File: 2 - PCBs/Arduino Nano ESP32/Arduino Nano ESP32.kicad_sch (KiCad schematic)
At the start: 27 parts, among them J1 USB4056-03-A, U2 MP9943GQ-Z, U3 GD25B128EWIGR

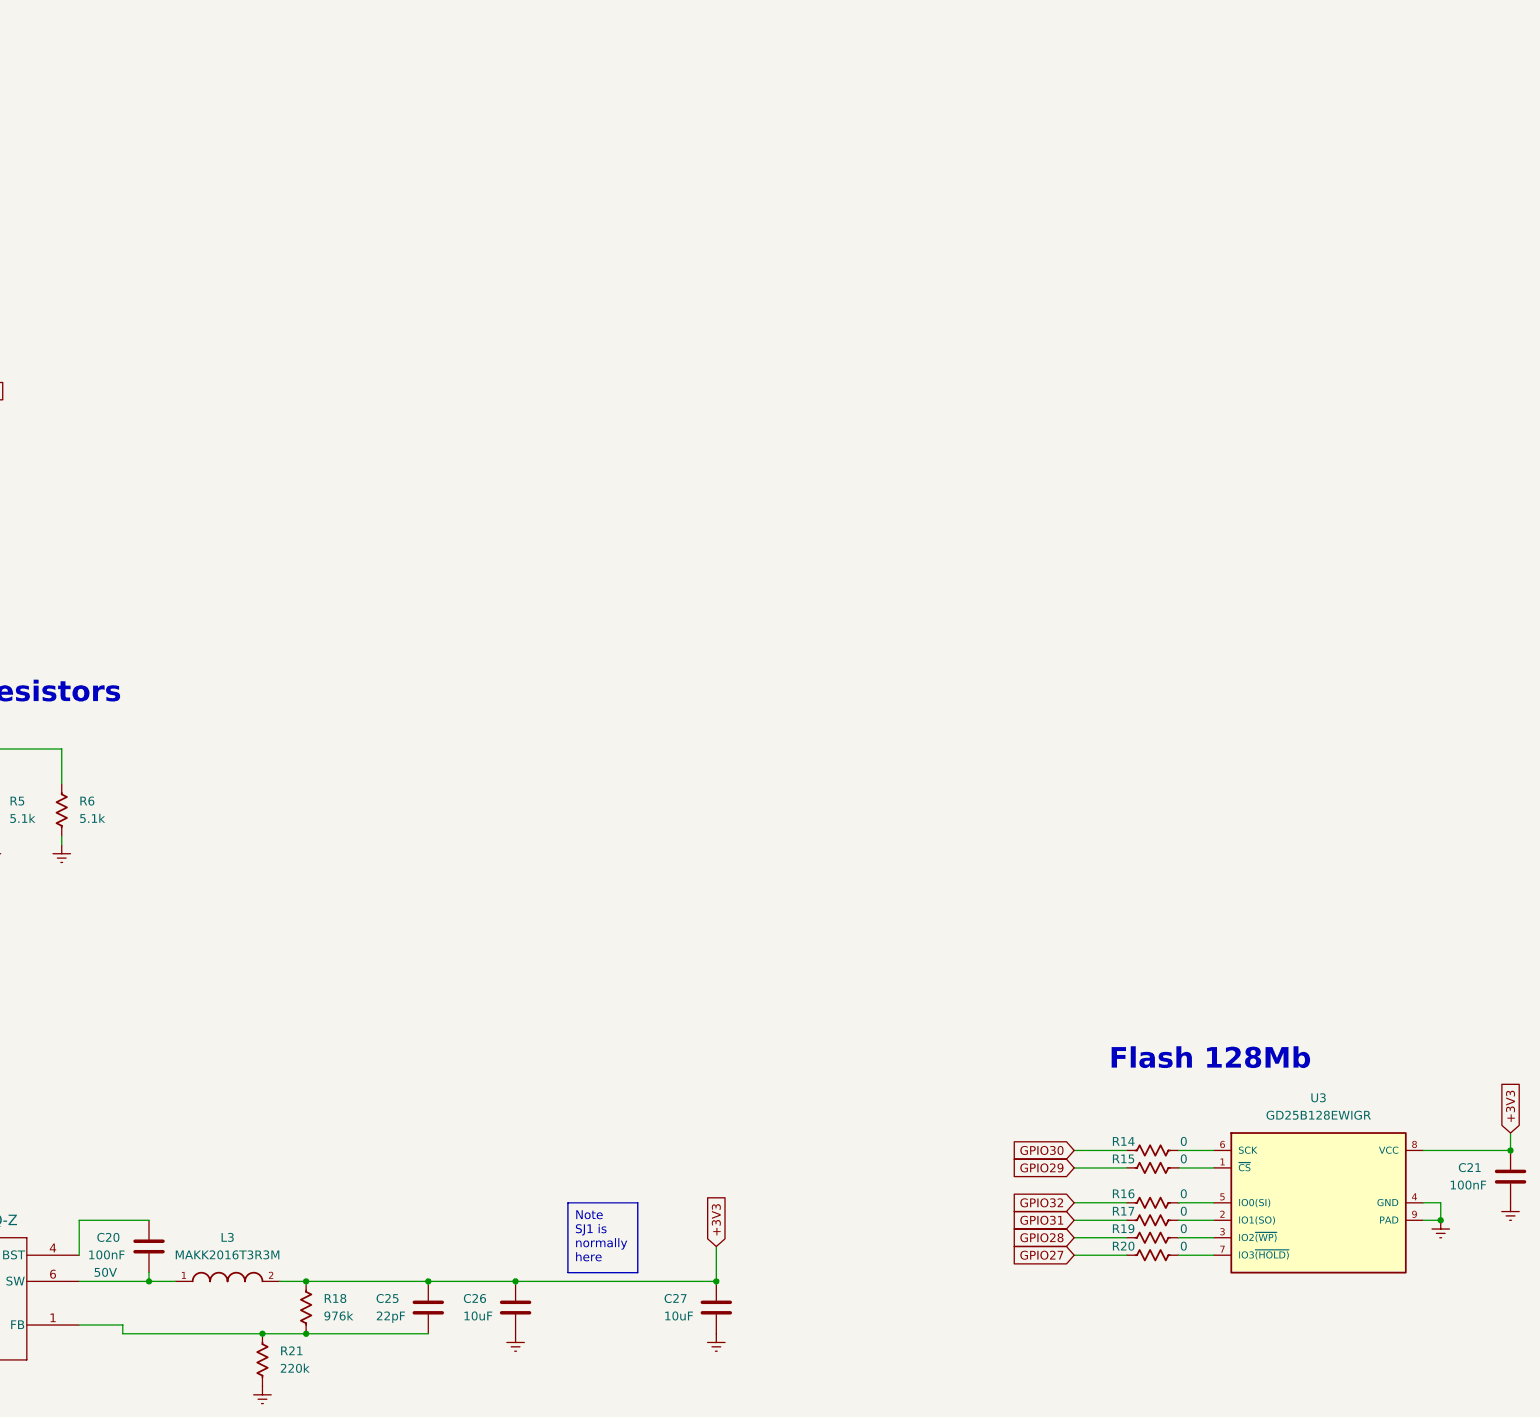
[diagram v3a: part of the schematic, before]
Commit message: Finished left side of SOC
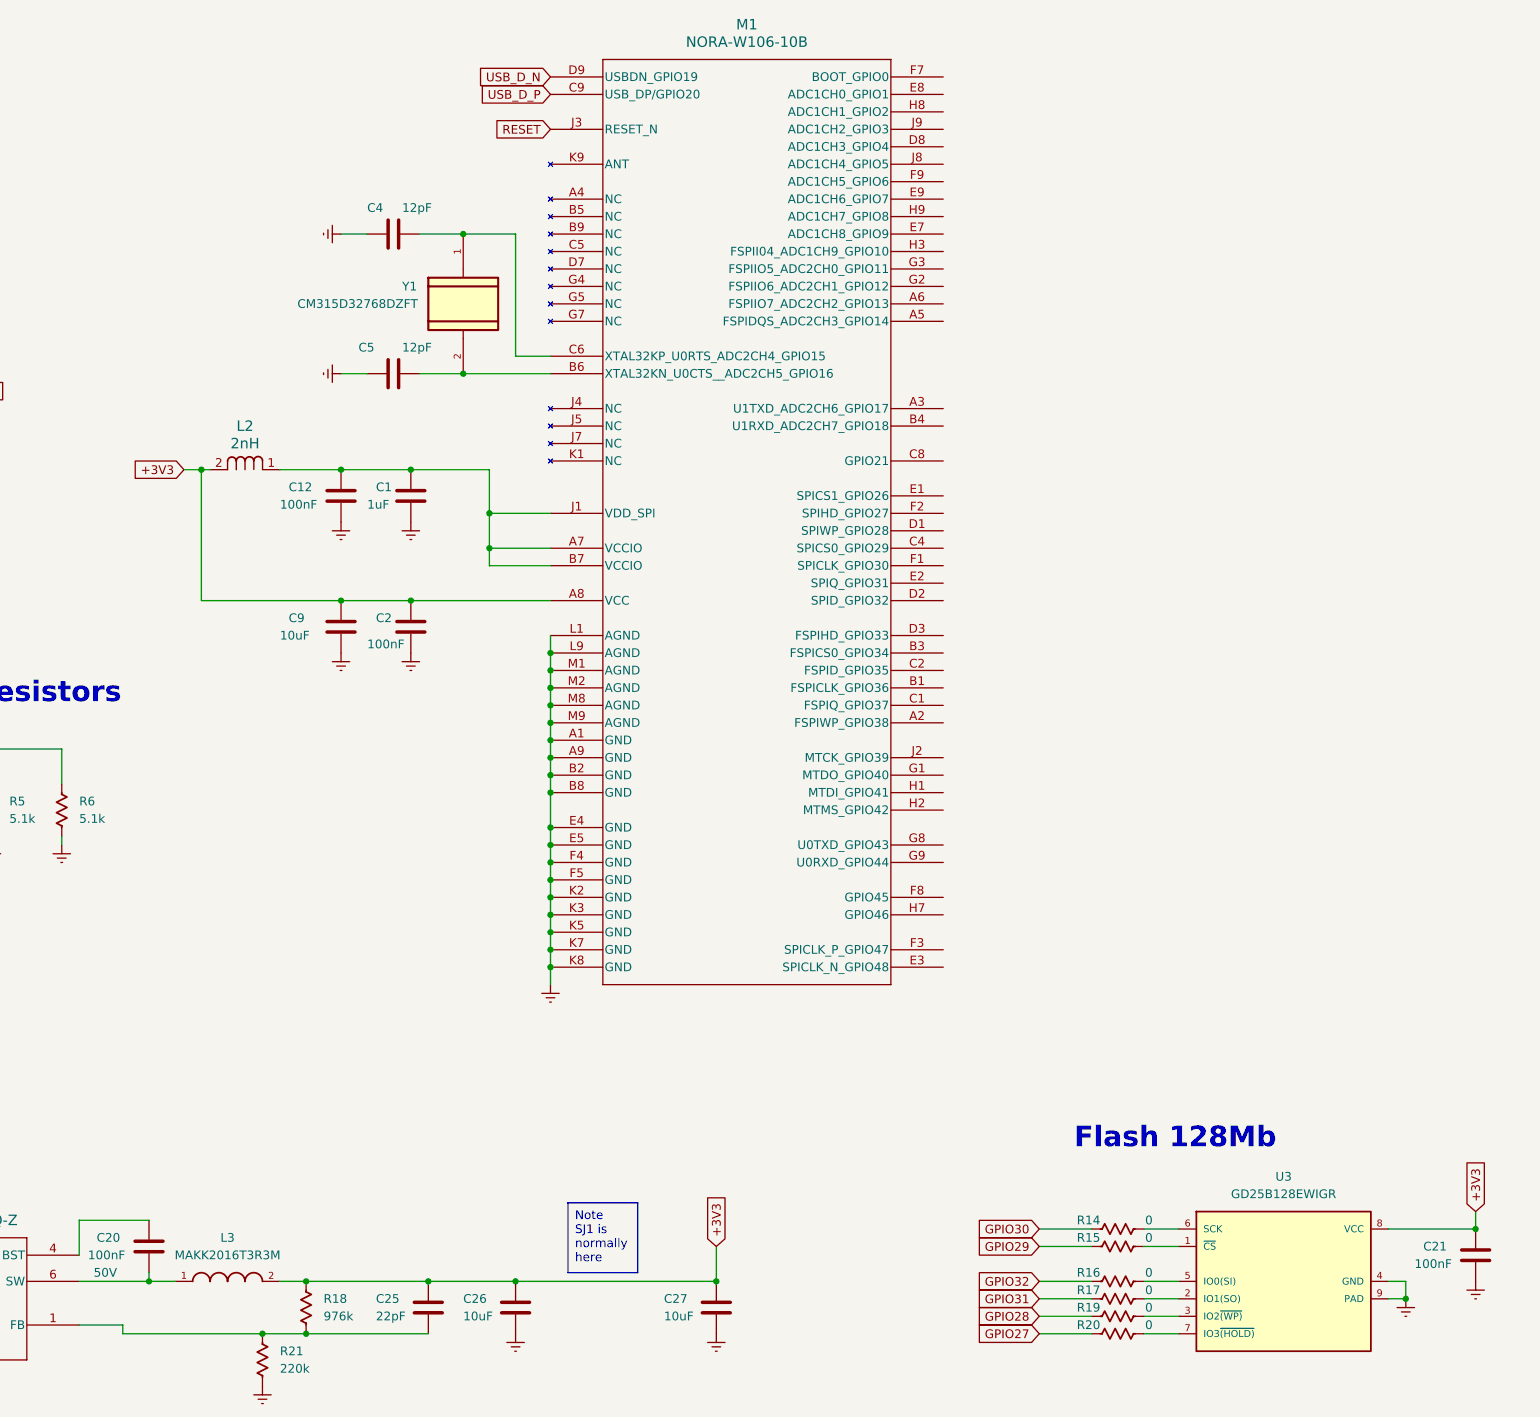
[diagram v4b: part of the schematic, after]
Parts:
- added C1: 1uF, Capacitor_SMD_AKL:C_0603_1608Metric, symbol Capacitor_US_AKL:C_0603
- added C12, C2: 100nF, Capacitor_SMD_AKL:C_0603_1608Metric, symbol Capacitor_US_AKL:C_0603
- added C4, C5: 12pF, Capacitor_SMD_AKL:C_0603_1608Metric, symbol Capacitor_US_AKL:C_0603
- added C9: 10uF, Capacitor_SMD_AKL:C_0603_1608Metric, symbol Capacitor_US_AKL:C_0603
- added L2: 2nH, 0603_inductor:0603_inductor, symbol 0603_inductor:0603_inductor
- added M1: NORA-W106-10B, NORA-W106-00B:NORA-W106-00B, symbol NORA_W106_00B:NORA-W106-00B
- added Y1: CM315D32768DZFT, CM315D32768DZFT:CM315D32768DZFT, symbol CM315D32768DZFT:CM315D32768DZFT
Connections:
- net +3V3: now also C2.1, C9.1, L2.2, M1.A8 (VCC)
- net Earth: now also C1.2, C12.2, C2.2, C4.2, C5.2, C9.2, M1.A1 (GND), M1.A9 (GND), M1.B2 (GND), M1.B8 (GND), M1.E4 (GND), M1.E5 (GND), M1.F4 (GND), M1.F5 (GND), M1.K2 (GND), M1.K3 (GND), M1.K5 (GND), M1.K7 (GND), M1.K8 (GND), M1.L1 (AGND), M1.L9 (AGND), M1.M1 (AGND), M1.M2 (AGND), M1.M8 (AGND), M1.M9 (AGND)
- net USB_D_N: now also M1.D9 (USBDN_GPIO19)
- net USB_D_P: now also M1.C9 (USB_DP/GPIO20)
- new net: C4.1, M1.C6 (XTAL32KP_U0RTS_ADC2CH4_GPIO15), Y1.1
- new net: C5.1, M1.B6 (XTAL32KN_U0CTS__ADC2CH5_GPIO16), Y1.2
- new net: C1.1, C12.1, L2.1, M1.A7 (VCCIO), M1.B7 (VCCIO), M1.J1 (VDD_SPI)
- new net RESET: M1.J3 (RESET_N)
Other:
- moved on the sheet: C21, R14, R15, R16, R17, R19, R20, U3

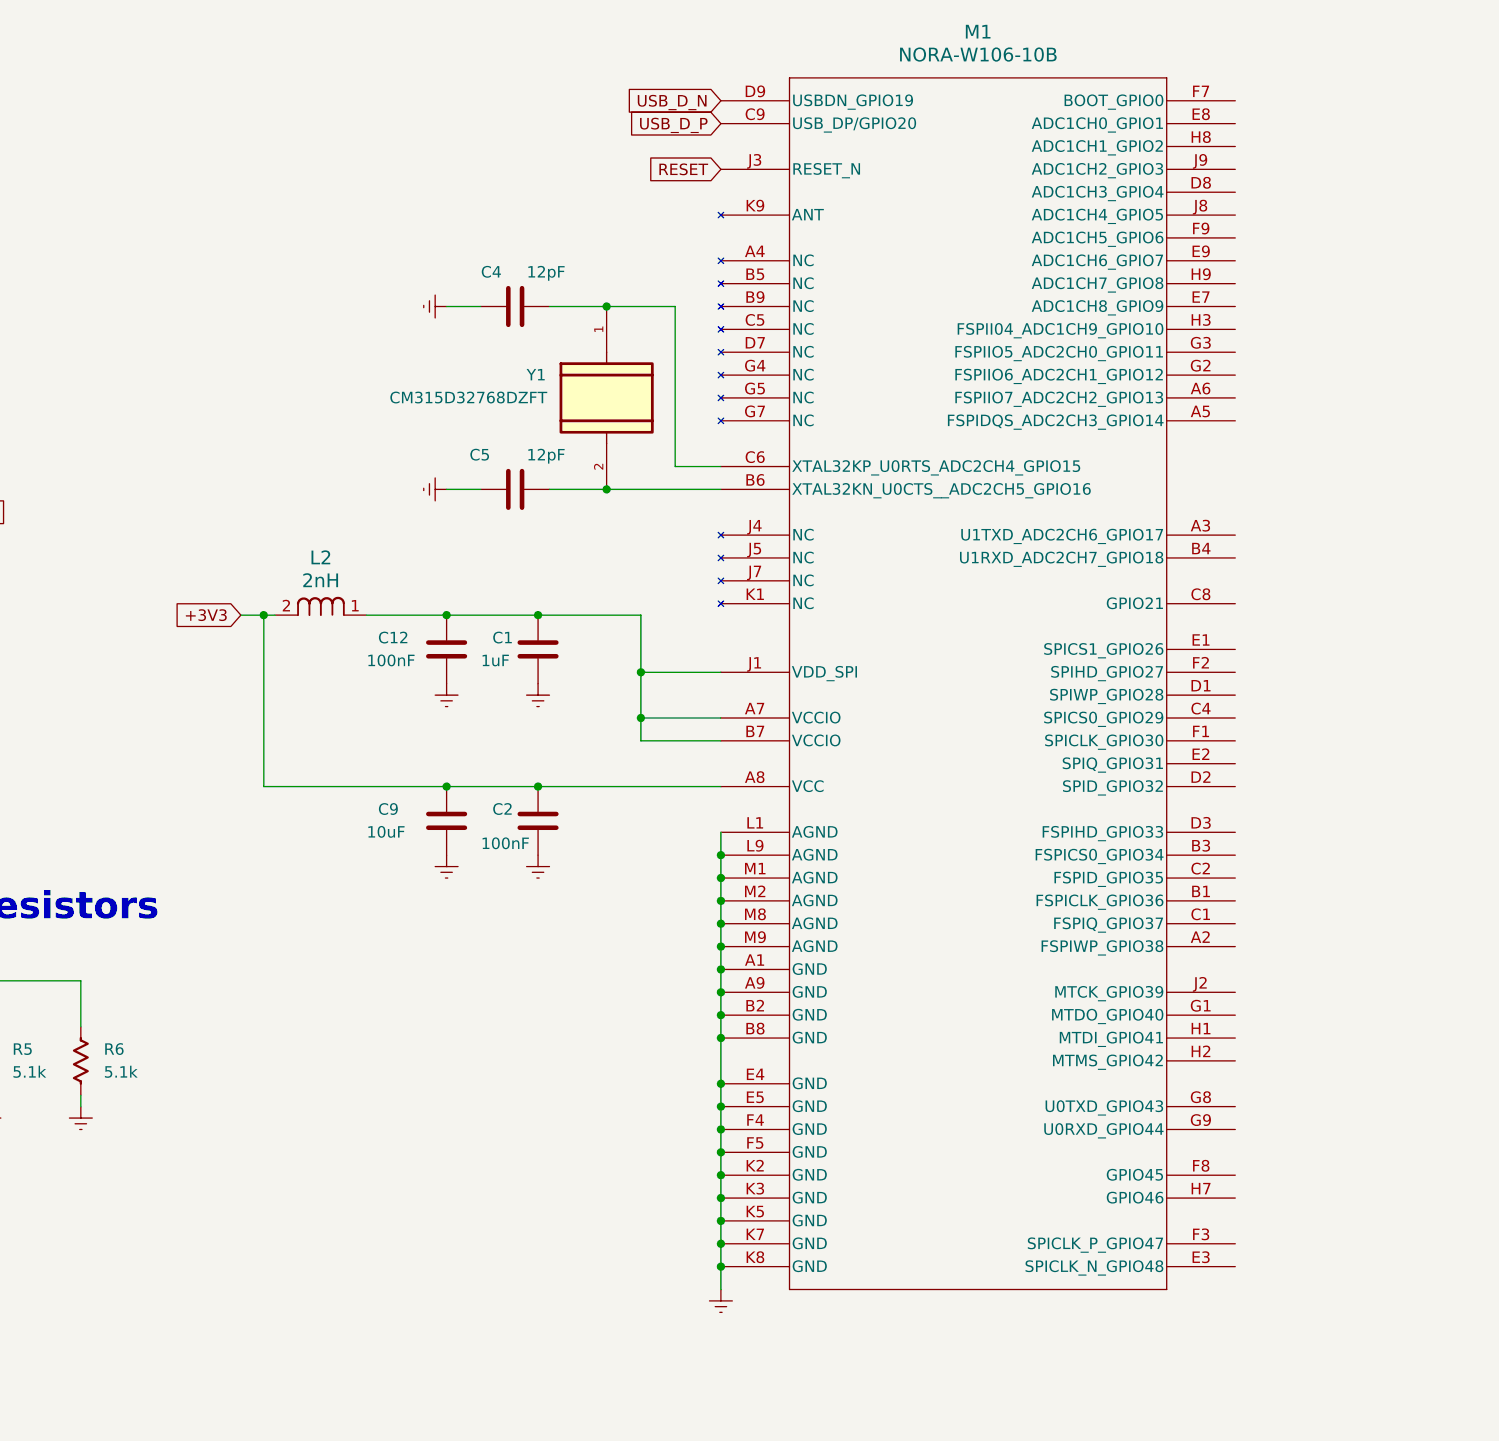
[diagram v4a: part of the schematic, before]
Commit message: finished SOC pinout schematic
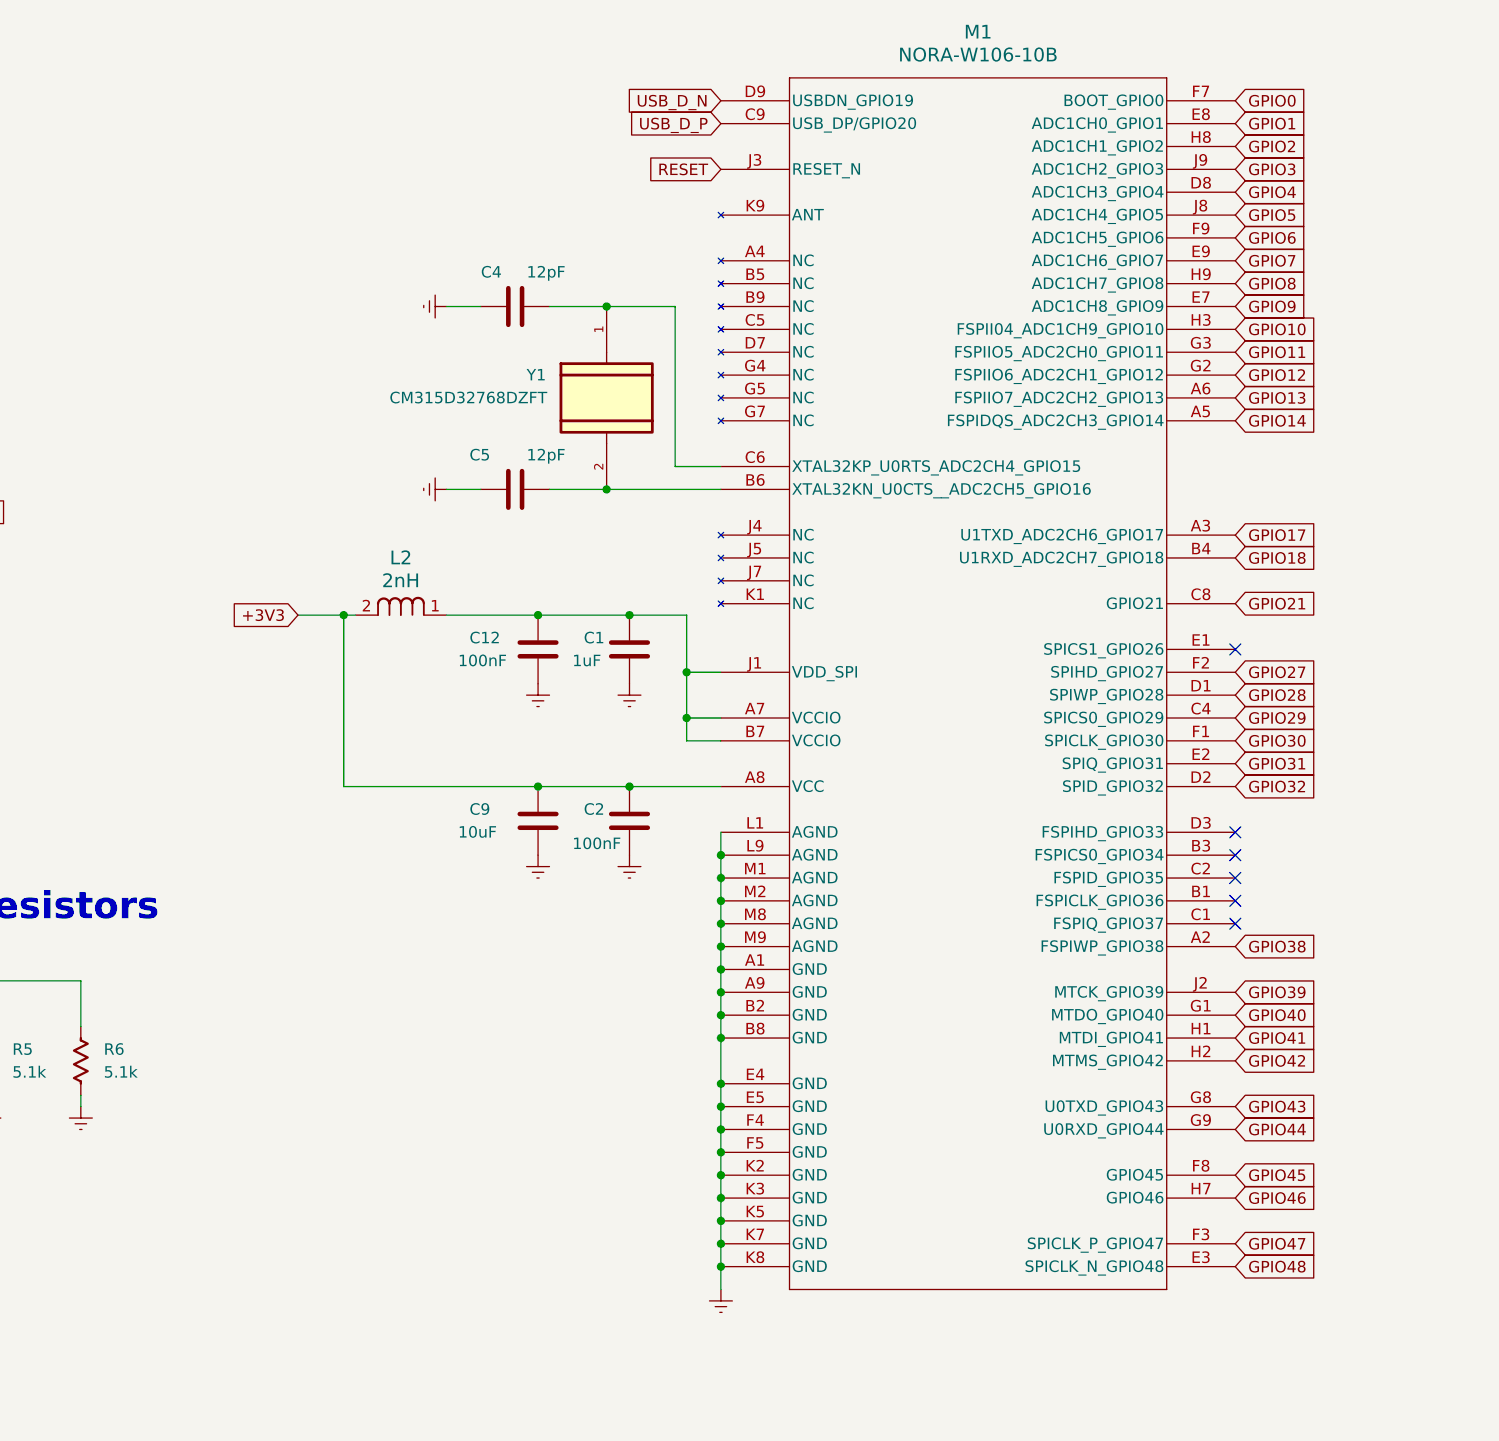
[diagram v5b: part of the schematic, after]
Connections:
- net GPIO27: now also M1.F2 (SPIHD_GPIO27)
- net GPIO28: now also M1.D1 (SPIWP_GPIO28)
- net GPIO29: now also M1.C4 (SPICS0_GPIO29)
- net GPIO30: now also M1.F1 (SPICLK_GPIO30)
- net GPIO31: now also M1.E2 (SPIQ_GPIO31)
- net GPIO32: now also M1.D2 (SPID_GPIO32)
- net GPIO38: now reaches M1.A2 (FSPIWP_GPIO38)
- net GPIO17: now reaches M1.A3 (U1TXD_ADC2CH6_GPIO17)
- net GPIO14: now reaches M1.A5 (FSPIDQS_ADC2CH3_GPIO14)
- net GPIO13: now reaches M1.A6 (FSPIIO7_ADC2CH2_GPIO13)
- net GPIO18: now reaches M1.B4 (U1RXD_ADC2CH7_GPIO18)
- net GPIO21: now reaches M1.C8 (GPIO21)
- net GPIO4: now reaches M1.D8 (ADC1CH3_GPIO4)
- net GPIO48: now reaches M1.E3 (SPICLK_N_GPIO48)
- net GPIO9: now reaches M1.E7 (ADC1CH8_GPIO9)
- net GPIO1: now reaches M1.E8 (ADC1CH0_GPIO1)
- net GPIO7: now reaches M1.E9 (ADC1CH6_GPIO7)
- net GPIO47: now reaches M1.F3 (SPICLK_P_GPIO47)
- net GPIO0: now reaches M1.F7 (BOOT_GPIO0)
- net GPIO45: now reaches M1.F8 (GPIO45)
- net GPIO6: now reaches M1.F9 (ADC1CH5_GPIO6)
- net GPIO40: now reaches M1.G1 (MTDO_GPIO40)
- net GPIO12: now reaches M1.G2 (FSPIIO6_ADC2CH1_GPIO12)
- net GPIO11: now reaches M1.G3 (FSPIIO5_ADC2CH0_GPIO11)
- net GPIO43: now reaches M1.G8 (U0TXD_GPIO43)
- net GPIO44: now reaches M1.G9 (U0RXD_GPIO44)
- net GPIO41: now reaches M1.H1 (MTDI_GPIO41)
- net GPIO42: now reaches M1.H2 (MTMS_GPIO42)
- net GPIO10: now reaches M1.H3 (FSPII04_ADC1CH9_GPIO10)
- net GPIO46: now reaches M1.H7 (GPIO46)
- net GPIO2: now reaches M1.H8 (ADC1CH1_GPIO2)
- net GPIO8: now reaches M1.H9 (ADC1CH7_GPIO8)
- net GPIO39: now reaches M1.J2 (MTCK_GPIO39)
- net GPIO5: now reaches M1.J8 (ADC1CH4_GPIO5)
- net GPIO3: now reaches M1.J9 (ADC1CH2_GPIO3)
- no-connect marks 15 -> 21
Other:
- moved on the sheet: C1, C12, C2, C9, L2
